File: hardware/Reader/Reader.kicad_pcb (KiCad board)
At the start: 4 copper layers, 53.3 x 125.1 mm, 126 parts, among them CN1 AHDF15A-KG-TAXB

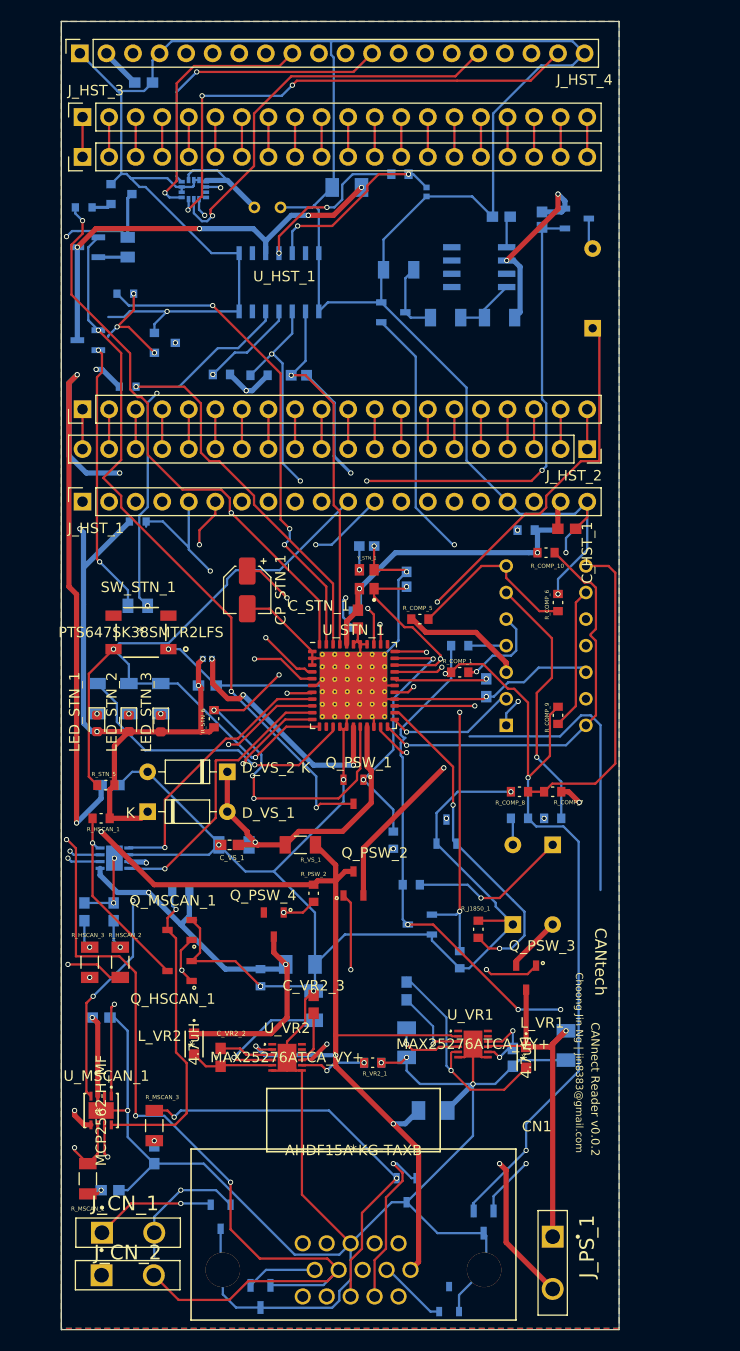
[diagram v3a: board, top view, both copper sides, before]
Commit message: Cleaned up a few sections for manufacturing
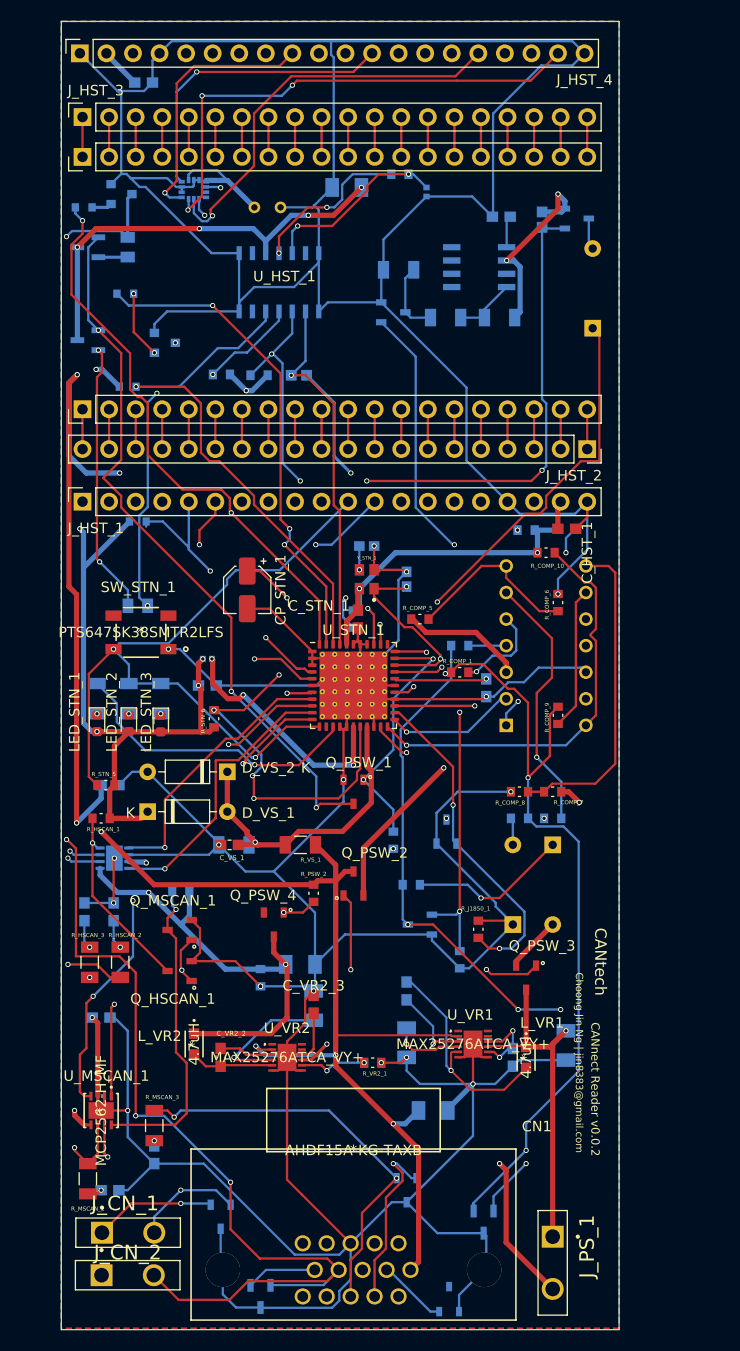
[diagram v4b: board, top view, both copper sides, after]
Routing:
- net (no net): track 29.5 -> 0.00 mm
- net Pin4_GnD_Chassis: track 655.0 -> 659.3 mm, vias 18 -> 17
- net Net-(Q_ISO_3-Pad1): track 9.73 -> 6.47 mm, vias 3 -> 2
- net Pin14_ISO15765_CAN_BUS_Low: track 87.7 -> 85.4 mm
- net /OBDII Interpreter/Medium Speed CAN Transceiver/MS_CAN_RX: track 46.7 -> 47.6 mm
